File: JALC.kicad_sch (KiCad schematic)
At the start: 5 parts, among them J1 Conn_01x03, U1 WeMos_D1_mini

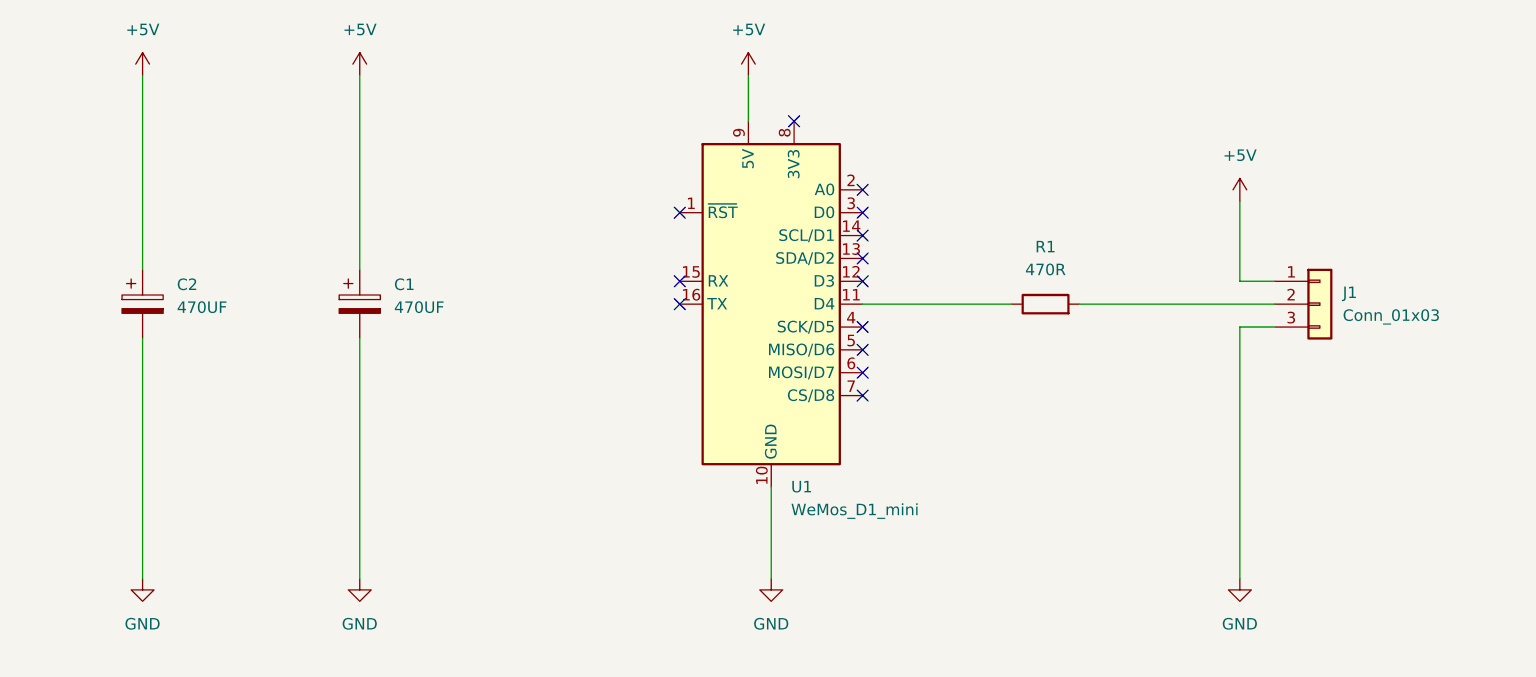
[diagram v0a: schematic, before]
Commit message: Added REV2.0 (ESP32-C3)
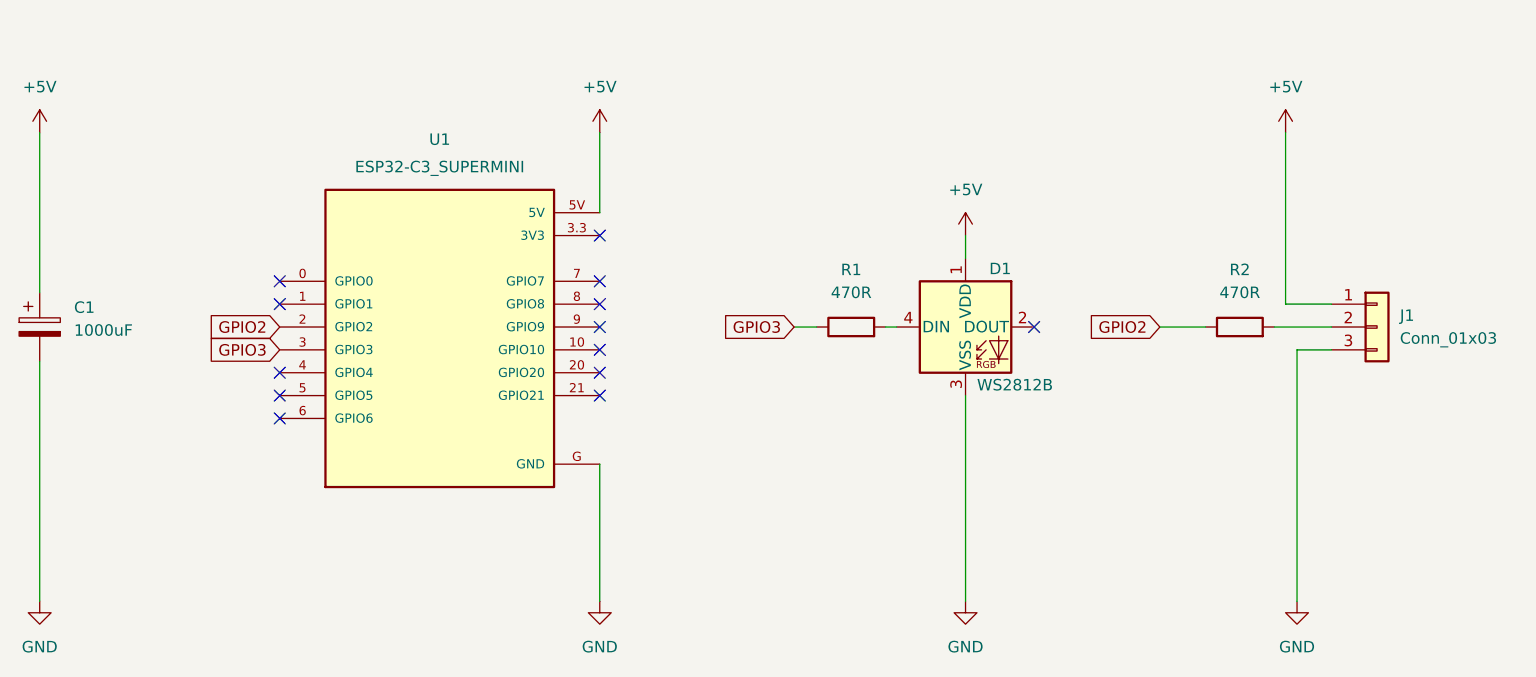
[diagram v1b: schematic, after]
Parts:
- removed C2: 470UF, Capacitor_SMD:CP_Elec_6.3x7.7, symbol Device:C_Polarized
- removed U1: WeMos_D1_mini, Module:WEMOS_D1_mini_light, symbol MCU_Module:WeMos_D1_mini
- added D1: WS2812B, LED_SMD:LED_WS2812B_PLCC4_5.0x5.0mm_P3.2mm, symbol LED:WS2812B
- added R2: 470R, Resistor_SMD:R_0805_2012Metric_Pad1.20x1.40mm_HandSolder, symbol Device:R
- added U1: ESP32-C3_SUPERMINI, MODULE_ESP32-C3_SUPERMINI:MODULE_ESP32-C3_SUPERMINI, symbol ESP32-C3_SUPERMINI:ESP32-C3_SUPERMINI
- C1: value 470UF -> 1000uF; footprint Capacitor_SMD:CP_Elec_6.3x7.7 -> Capacitor_Tantalum_SMD:CP_EIA-7343-43_Kemet-X
- J1: footprint Connector_PinHeader_2.54mm:PinHeader_1x03_P2.54mm_Vertical -> SolderConnector:SolderConnector
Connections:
- net +5V: now also D1.1 (VDD), U1.5V
- net GND: now also D1.3 (VSS), U1.G (GND)
- net GPIO3: now reaches R1.1
- net GPIO3: now also U1.3 (GPIO3)
- net at R1.2: now also D1.4 (DIN); no longer J1.2 (Pin_2)
- new net: J1.2 (Pin_2), R2.2
- new net GPIO2: R2.1, U1.2 (GPIO2)
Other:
- moved on the sheet: C1, J1, R1
